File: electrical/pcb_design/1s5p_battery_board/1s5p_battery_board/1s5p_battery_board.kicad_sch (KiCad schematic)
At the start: 15 parts, among them U1 STM32L452RCTx

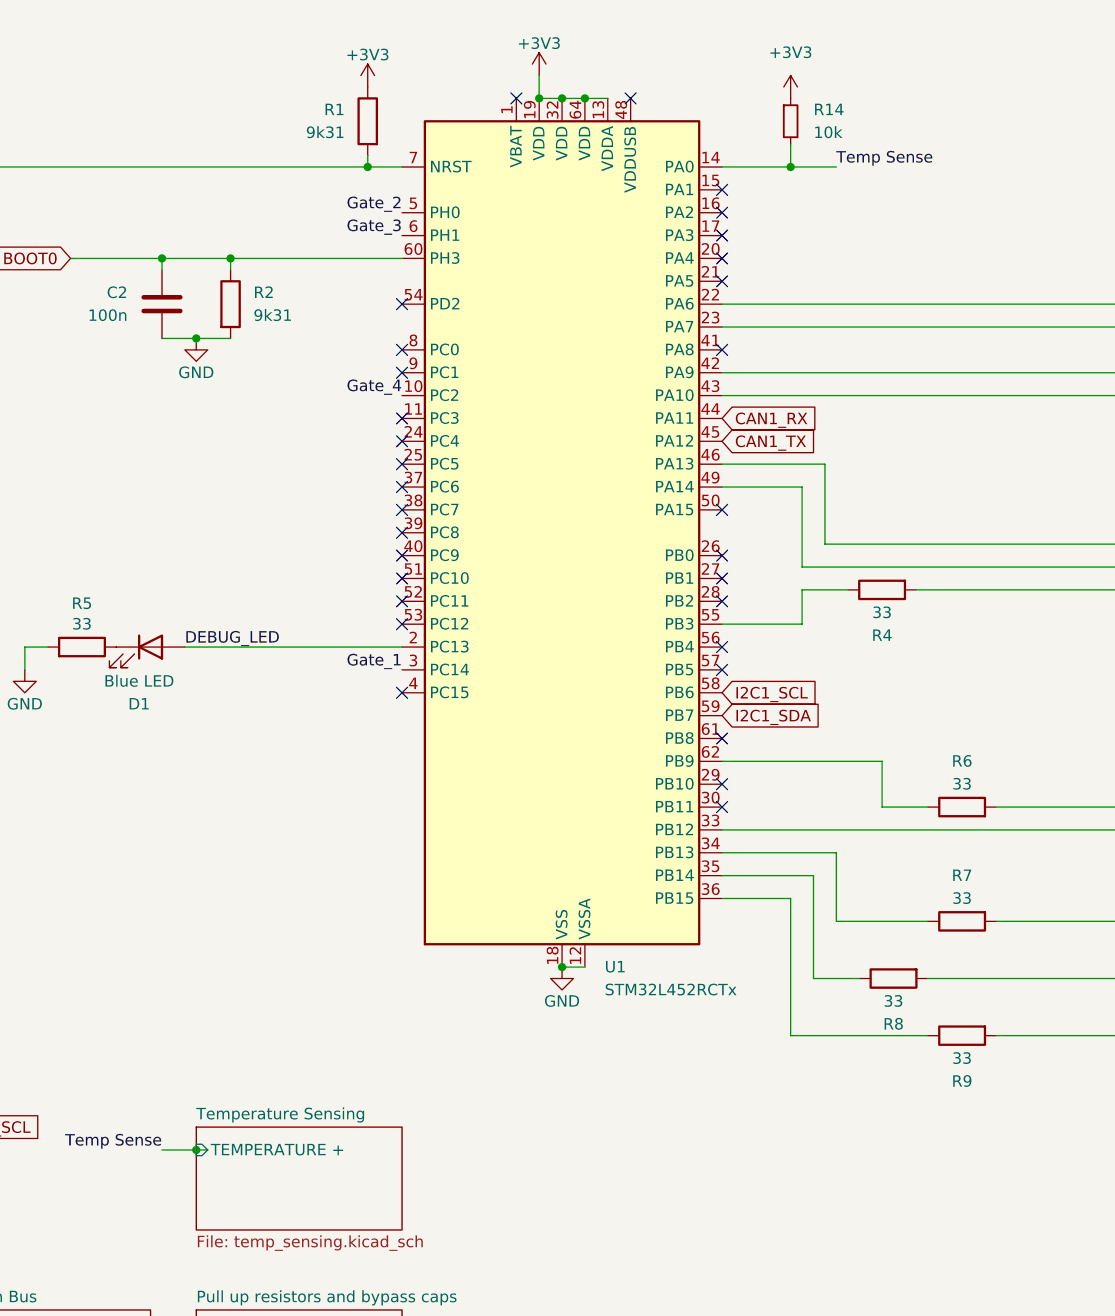
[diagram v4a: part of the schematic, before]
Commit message: general layout with new board shape, correct bus connector distance, no thermistor bypass, no board power plug
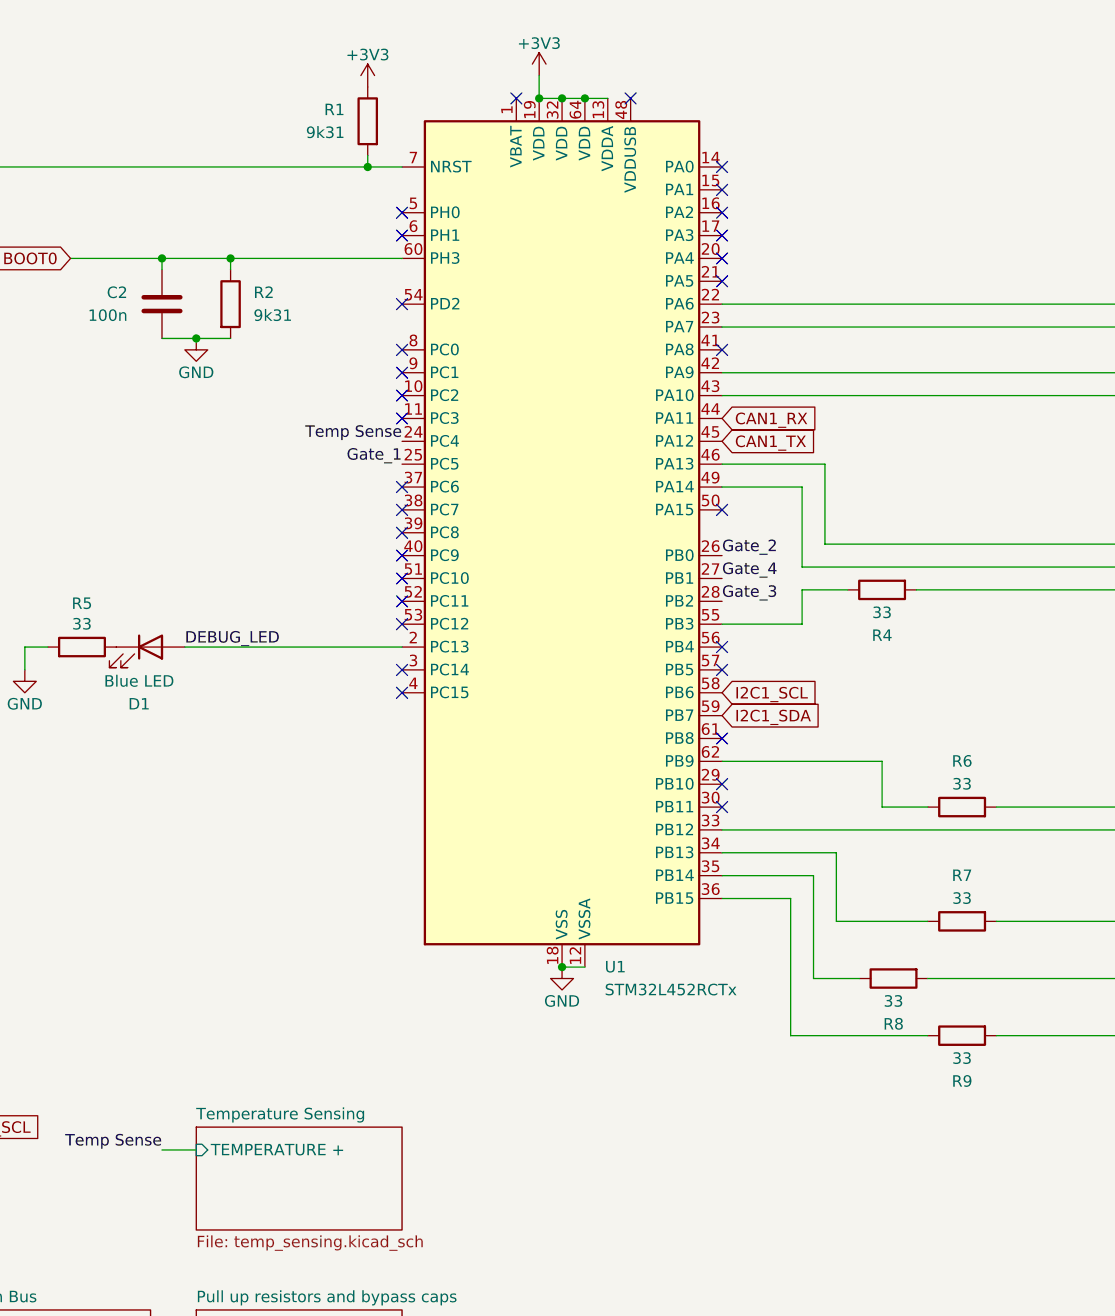
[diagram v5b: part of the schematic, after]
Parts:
- removed R14: 10k, footprints:Nondescript_R_0402_1005Metric, symbol Device:R_Small
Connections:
- net Gate_1: now also U1.25 (PC5); no longer U1.3 (PC14)
- net Gate_2: now also U1.26 (PB0); no longer U1.5 (PH0)
- net Gate_3: now also U1.28 (PB2); no longer U1.6 (PH1)
- net Gate_4: now also U1.27 (PB1); no longer U1.10 (PC2)
- net Temp Sense: now also U1.24 (PC4); no longer U1.14 (PA0)
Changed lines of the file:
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@@
-	)
-	(junction
-		(at 96.52 138.43)
-		(diameter 0)
-		(color 0 0 0 0)
-	)
-	(junction
-		(at 162.56 29.21)
-		(diameter 0)
-		(color 0 0 0 0)
 	)
 	(junction
@@
 	)
 	(no_connect
-		(at 154.94 72.39)
+		(at 119.38 36.83)
 	)
 	(no_connect
@@
 	)
 	(no_connect
-		(at 154.94 74.93)
-	)
-	(no_connect
 		(at 119.38 67.31)
 	)
@@
 	)
 	(no_connect
-		(at 154.94 77.47)
-	)
-	(no_connect
-		(at 119.38 59.69)
+		(at 154.94 29.21)
 	)
 	(no_connect
@@
 	)
 	(no_connect
-		(at 119.38 62.23)
-	)
-	(no_connect
 		(at 154.94 82.55)
 	)
@@
 	)
 	(no_connect
+		(at 119.38 85.09)
+	)
+	(no_connect
 		(at 119.38 44.45)
 	)
 	(no_connect
+		(at 119.38 34.29)
+	)
+	(no_connect
+		(at 119.38 54.61)
+	)
+	(no_connect
 		(at 119.38 52.07)
 	)
@@
 	(wire
 		(pts
-			(xy 162.56 29.21) (xy 167.64 29.21)
-		)
-		(stroke
-			(width 0)
-			(type default)
-		)
-	)
-	(wire
-		(pts
 			(xy 163.83 80.01) (xy 154.94 80.01)
 		)
@@
 	(wire
 		(pts
-			(xy 97.79 138.43) (xy 96.52 138.43)
-		)
-		(stroke
-			(width 0)
-			(type default)
-		)
-	)
-	(wire
-		(pts
 			(xy 228.6 113.03) (xy 185.42 113.03)
 		)
@@
 	(wire
 		(pts
-			(xy 96.52 138.43) (xy 92.71 138.43)
-		)
-		(stroke
-			(width 0)
-			(type default)
-		)
-	)
-	(wire
-		(pts
-			(xy 162.56 26.67) (xy 162.56 29.21)
-		)
-		(stroke
-			(width 0)
-			(type default)
-		)
-	)
-	(wire
-		(pts
 			(xy 115.57 27.94) (xy 115.57 29.21)
 		)
@@
 	(wire
 		(pts
-			(xy 154.94 29.21) (xy 162.56 29.21)
-		)
-		(stroke
-			(width 0)
-			(type default)
-		)
-	)
-	(wire
-		(pts
 			(xy 68.58 137.16) (xy 64.77 137.16)
 		)
@@
 	(wire
 		(pts
+			(xy 92.71 138.43) (xy 96.52 138.43)
+		)
+		(stroke
+			(width 0)
+			(type default)
+		)
+	)
+	(wire
+		(pts
 			(xy 257.81 24.13) (xy 257.81 31.75)
 		)
@@
 	)
 	(label "Gate_2"
-		(at 119.38 34.29 180)
+		(at 154.94 72.39 0)
+		(effects
+			(font
+				(size 1.27 1.27)
+			)
+			(justify left bottom)
+		)
+	)
+	(label "Gate_4"
+		(at 154.94 74.93 0)
+		(effects
+			(font
+				(size 1.27 1.27)
+			)
+			(justify left bottom)
+		)
+	)
+	(label "Temp Sense"
+		(at 119.38 59.69 180)
 		(effects
 			(font
@@
 			)
 			(justify right bottom)
-		)
-	)
-	(label "Gate_4"
-		(at 119.38 54.61 180)
-		(effects
-			(font
-				(size 1.27 1.27)
-			)
-			(justify right bottom)
-		)
-	)
-	(label "Temp Sense"
-		(at 167.64 29.21 0)
-		(effects
-			(font
-				(size 1.27 1.27)
-			)
-			(justify left bottom)
 		)
 	)
@@
 	)
 	(label "Gate_1"
-		(at 119.38 85.09 180)
+		(at 119.38 62.23 180)
 		(effects
 			(font
@@
 	)
 	(label "Gate_3"
-		(at 119.38 36.83 180)
-		(effects
-			(font
-				(size 1.27 1.27)
-			)
-			(justify right bottom)
+		(at 154.94 77.47 0)
+		(effects
+			(font
+				(size 1.27 1.27)
+			)
+			(justify left bottom)
 		)
 	)
@@
 	)
 	(symbol
-		(lib_id "Device:R_Small")
-		(at 162.56 24.13 0)
-		(unit 1)
-		(exclude_from_sim no)
-		(in_bom yes)
-		(on_board yes)
-		(dnp no)
-		(fields_autoplaced yes)
-		(property "Reference" "R14"
-			(at 165.1 22.8599 0)
-			(effects
-				(font
-					(size 1.27 1.27)
-				)
-				(justify left)
-			)
-		)
-		(property "Value" "10k"
-			(at 165.1 25.3999 0)
-			(effects
-				(font
-					(size 1.27 1.27)
-				)
-				(justify left)
-			)
-		)
-		(property "Footprint" "footprints:Nondescript_R_0402_1005Metric"
-			(at 162.56 24.13 0)
-			(effects
-				(font
-					(size 1.27 1.27)
-				)
-				(hide yes)
-			)
-		)
-		(property "Datasheet" "~"
-			(at 162.56 24.13 0)
-			(effects
-				(font
-					(size 1.27 1.27)
-				)
-				(hide yes)
-			)
-		)
-		(property "Description" "Resistor, small symbol"
-			(at 162.56 24.13 0)
-			(effects
-				(font
-					(size 1.27 1.27)
-				)
-				(hide yes)
-			)
-		)
-		(pin "2"
-		)
-		(pin "1"
-		)
-		(instances
-			(project ""
-				(path "/4447b8ba-2ae9-4ff2-bb5c-b43a54dd7059"
-					(reference "R14")
-					(unit 1)
-				)
-			)
-		)
-	)
-	(symbol
 		(lib_id "power:GND")
 		(at 64.77 36.83 0)
@@
 					(unit 1)
 				)
-			)
-		)
-	)
-	(symbol
-		(lib_id "power:+3V3")
-		(at 162.56 21.59 0)
-		(unit 1)
-		(exclude_from_sim no)
-		(in_bom yes)
-		(on_board yes)
-		(dnp no)
-		(fields_autoplaced yes)
-		(property "Reference" "#PWR053"
-			(at 162.56 25.4 0)
-			(effects
-				(font
-					(size 1.27 1.27)
-				)
-				(hide yes)
-			)
-		)
-		(property "Value" "+3V3"
-			(at 162.56 16.51 0)
-			(effects
-				(font
-					(size 1.27 1.27)
-				)
-			)
-		)
-		(property "Footprint" ""
-			(at 162.56 21.59 0)
-			(effects
-				(font
-					(size 1.27 1.27)
-				)
-				(hide yes)
-			)
-		)
-		(property "Datasheet" ""
-			(at 162.56 21.59 0)
-			(effects
-				(font
-					(size 1.27 1.27)
-				)
-				(hide yes)
-			)
-		)
-		(property "Description" "Power symbol creates a global label with name \"+3V3\""
-			(at 162.56 21.59 0)
-			(effects
-				(font
-					(size 1.27 1.27)
-				)
-				(hide yes)
-			)
-		)
-		(pin "1"
-		)
-		(instances
-			(project ""
-				(path "/4447b8ba-2ae9-4ff2-bb5c-b43a54dd7059"
-					(reference "#PWR053")
-					(unit 1)
-				)

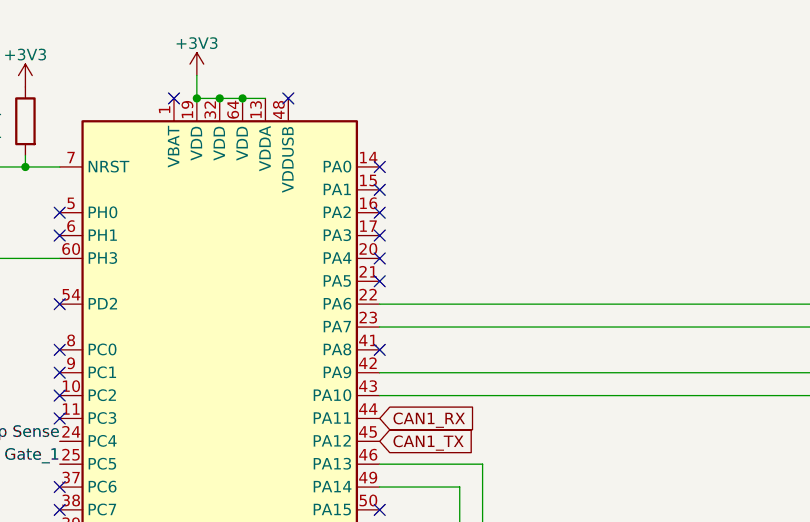
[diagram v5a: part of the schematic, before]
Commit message: add PA0 as additional board ID, add signal wires in layout, start power wiring in layout
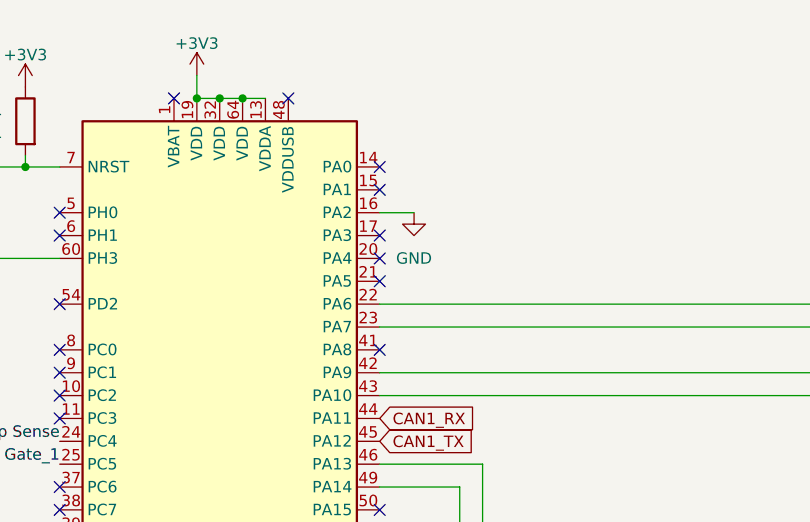
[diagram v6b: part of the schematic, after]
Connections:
- net GND: now also U1.16 (PA2)
- no-connect marks 31 -> 30
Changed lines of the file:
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@@
 	)
 	(no_connect
-		(at 154.94 34.29)
-	)
-	(no_connect
 		(at 154.94 100.33)
 	)
@@
 	(wire
 		(pts
+			(xy 154.94 34.29) (xy 158.75 34.29)
+		)
+		(stroke
+			(width 0)
+			(type default)
+		)
+	)
+	(wire
+		(pts
 			(xy 213.36 71.12) (xy 228.6 71.12)
 		)
@@
 					(unit 1)
 				)
+			)
+		)
+	)
+	(symbol
+		(lib_id "power:GND")
+		(at 158.75 34.29 0)
+		(unit 1)
+		(exclude_from_sim no)
+		(in_bom yes)
+		(on_board yes)
+		(dnp no)
+		(fields_autoplaced yes)
+		(property "Reference" "#PWR026"
+			(at 158.75 40.64 0)
+			(effects
+				(font
+					(size 1.27 1.27)
+				)
+				(hide yes)
+			)
+		)
+		(property "Value" "GND"
+			(at 158.75 39.37 0)
+			(effects
+				(font
+					(size 1.27 1.27)
+				)
+			)
+		)
+		(property "Footprint" ""
+			(at 158.75 34.29 0)
+			(effects
+				(font
+					(size 1.27 1.27)
+				)
+				(hide yes)
+			)
+		)
+		(property "Datasheet" ""
+			(at 158.75 34.29 0)
+			(effects
+				(font
+					(size 1.27 1.27)
+				)
+				(hide yes)
+			)
+		)
+		(property "Description" "Power symbol creates a global label with name \"GND\" , ground"
+			(at 158.75 34.29 0)
+			(effects
+				(font
+					(size 1.27 1.27)
+				)
+				(hide yes)
+			)
+		)
+		(pin "1"
+		)
+		(instances
+			(project ""
+				(path "/4447b8ba-2ae9-4ff2-bb5c-b43a54dd7059"
+					(reference "#PWR026")
+					(unit 1)
+				)
